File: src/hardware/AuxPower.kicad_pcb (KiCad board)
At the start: 2 copper layers, 90 x 90 mm, 103 parts, among them J1 MC 1,5/2, J10 MC 1,5/4, J11 S3B-XH-A, J12 S3B-XH-A, J13 S3B-XH-A, J14 S3B-XH-A, J15 S3B-XH-A, J16 B3B-XH-A, J17 B4B-XH-A, J2 MC 1,5/2, J3 MC 1,5/2, J4 MC 1,5/2, J5 MC 1,5/2, J6 MC 1,5/4, J7 MC 1,5/4, J8 MC 1,5/4, J9 MC 1,5/4, K1 AQZ202G, K2 AQZ202G, K3 AQZ202G, K4 AQZ202G, K5 AQZ202G, U1 ZXCT1009, U2 ZXCT1009, U3 ZXCT1009, U4 ZXCT1009, U5 ZXCT1009, U6 PIC18F26K83, U7 PI4IOE5V6416, U8 MCP9701

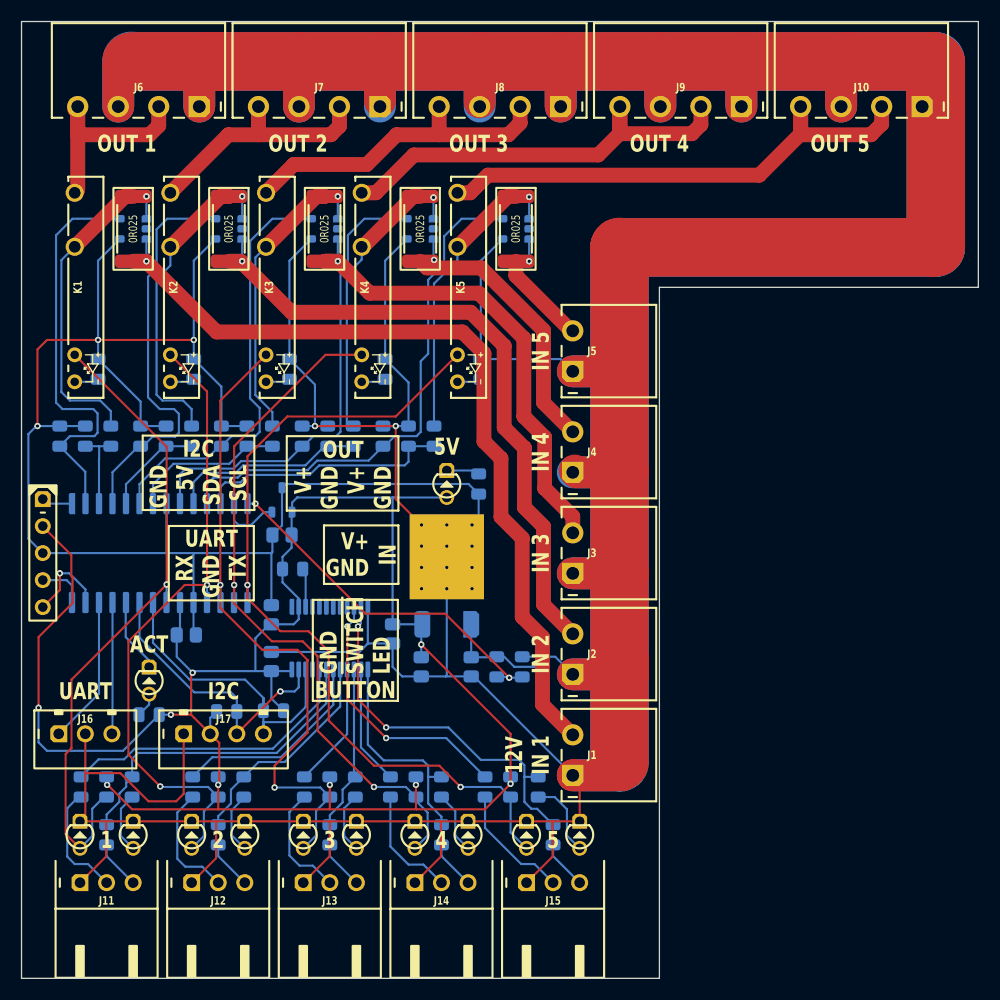
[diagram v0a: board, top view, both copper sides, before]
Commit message: Refactored the whole board to have switches in airflow direction
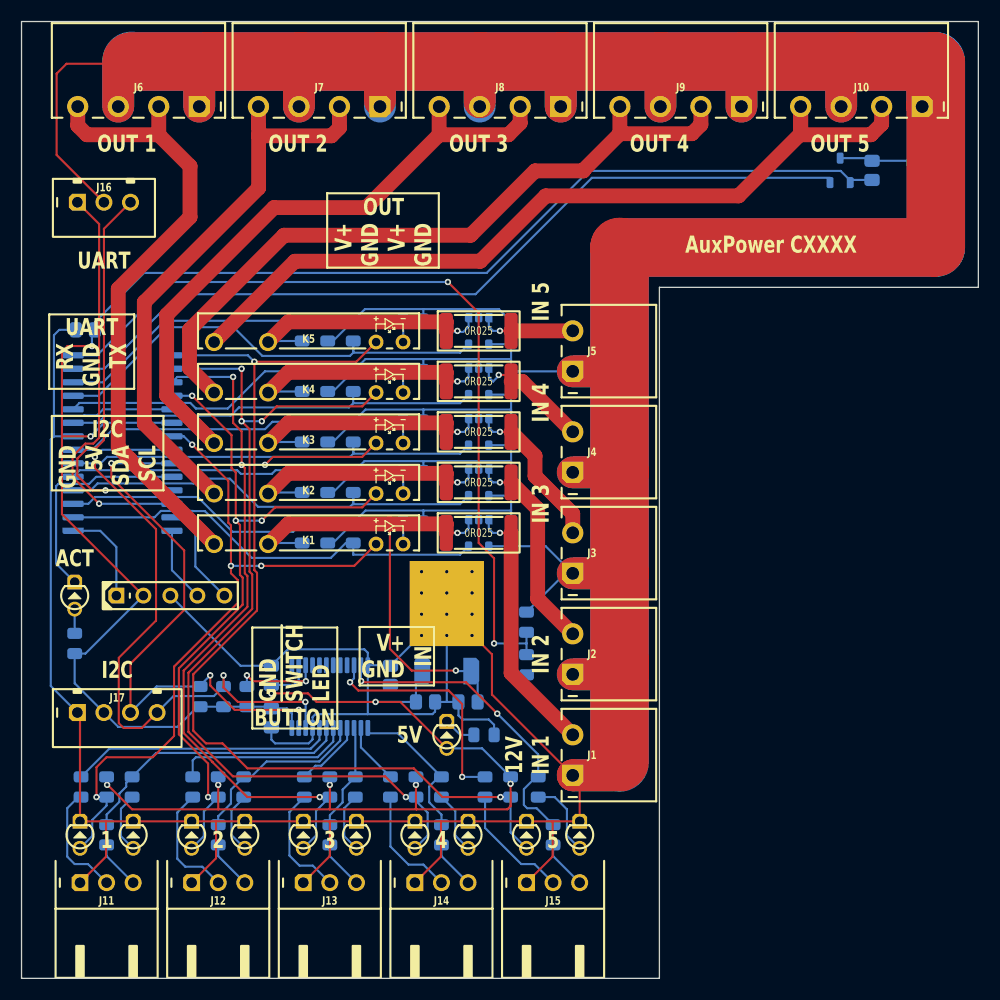
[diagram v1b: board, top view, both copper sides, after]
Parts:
- ICSP: footprint Medo64:ICSP PIC Pogo (5w) -> Medo64:ICSP PIC Pogo DS (5w)
- moved C4 65.2 mm to (95.0, 29.0), turned to 90 degrees
- moved U8 61.0 mm to (92.0, 29.0)
- moved J16 50.0 mm to (22.8, 32.0)
- moved R1 43.3 mm to (58.0, 63.1), turned to 180 degrees
- moved U1 43.3 mm to (58.0, 63.1), turned to -90 degrees
- moved R2 33.5 mm to (58.0, 58.4), turned to 180 degrees
- moved U2 33.5 mm to (58.0, 58.4), turned to -90 degrees
- moved R16 33.0 mm to (51.9, 62.1), turned to 0 degrees
- moved K1 32.7 mm to (42.0, 64.2), turned to 180 degrees
- moved C5 30.2 mm to (21.0, 44.0), turned to 180 degrees
- moved R11 29.1 mm to (46.2, 63.1)
- moved R41 24.5 mm to (43.8, 63.1), turned to -90 degrees
- moved R3 24.0 mm to (58.0, 53.6), turned to 180 degrees
- moved U3 24.0 mm to (58.0, 53.6), turned to -90 degrees
- moved R31 23.6 mm to (58.5, 82.1), turned to 180 degrees
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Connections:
- C7 pad 2: INPUT1 -> INPUT1'
- VR1 pad 1: INPUT1 -> INPUT1'
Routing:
- net ADC_TEMPERATURE: track 5.82 -> 79.1 mm
- net INPUT1: track 95.6 -> 31.8 mm
- net 5V: track 192.9 -> 249.7 mm
- net ADC_VOLTAGE_IN: track 33.8 -> 79.1 mm
- net INPUT2: track 61.1 -> 19.7 mm
- net OUTPUT1: track 21.1 -> 58.7 mm
- net I2C_SCL: track 29.7 -> 61.0 mm, vias 0 -> 3
- net OUTPUT2: track 23.0 -> 53.5 mm
- net INPUT3: track 44.8 -> 15.1 mm
- net OUTPUT5: track 49.5 -> 78.2 mm
- net OUTPUT3: track 30.8 -> 58.9 mm
- net I2C_SDA: track 27.5 -> 54.9 mm, vias 1 -> 3
- net OUTPUT4: track 41.3 -> 67.2 mm
- net UART_TX: track 12.3 -> 37.7 mm, vias 0 -> 1
- net UART_RX: track 13.9 -> 38.6 mm, vias 0 -> 1
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
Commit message: Added mounting hole
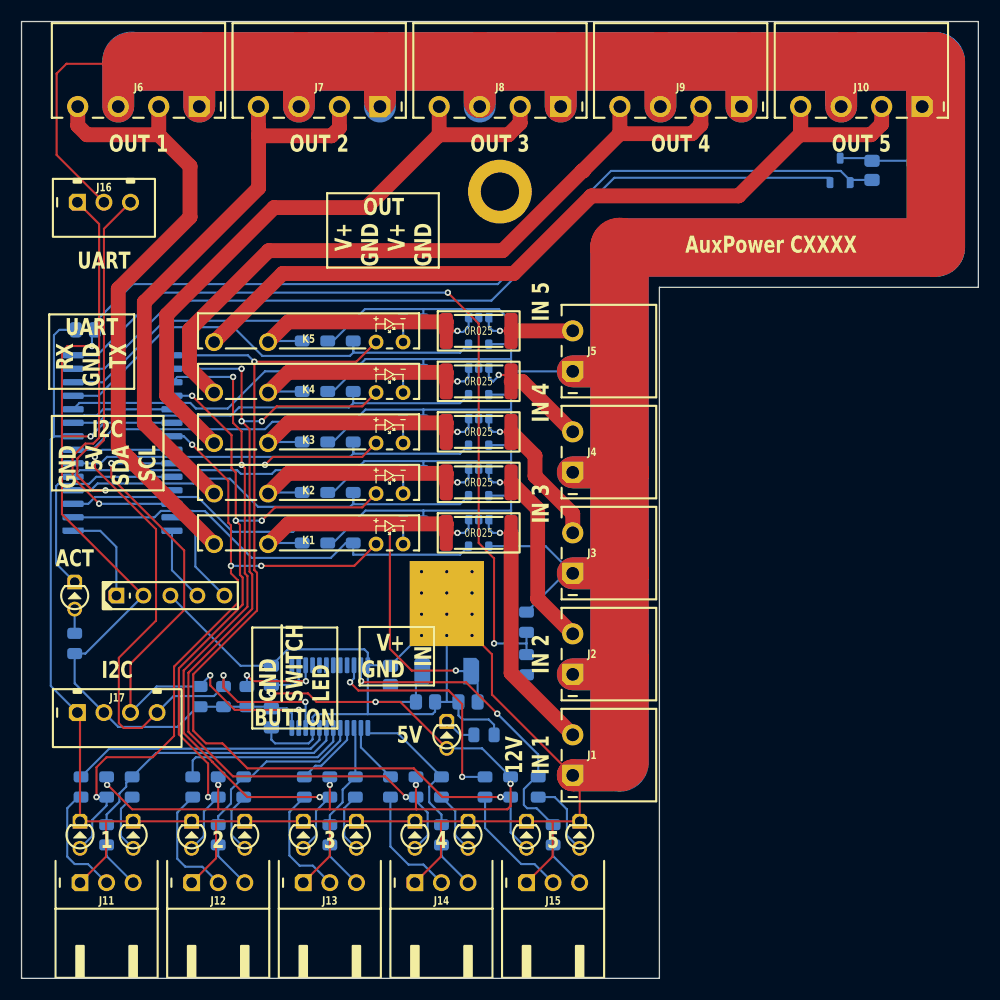
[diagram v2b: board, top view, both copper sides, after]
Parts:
- added MH1: M3, Medo64:MH M3, F.Cu at (60.0, 31.0)
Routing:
- net ADC_VOLTAGE_IN: track 79.1 -> 77.6 mm
